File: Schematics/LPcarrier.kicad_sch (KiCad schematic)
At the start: 46 parts, among them J284 Conn_01x04, J48 Conn_01x03, J49 Conn_01x04, J75 Conn_01x04, U241 LM78L05, U247 AMS1117-3.3, U248 PCF8574, U33 ADG409, U34 MCP4728, U35 ADG1204, U36 ADG1204, U55 TMUX6219, U57 TMUX6219

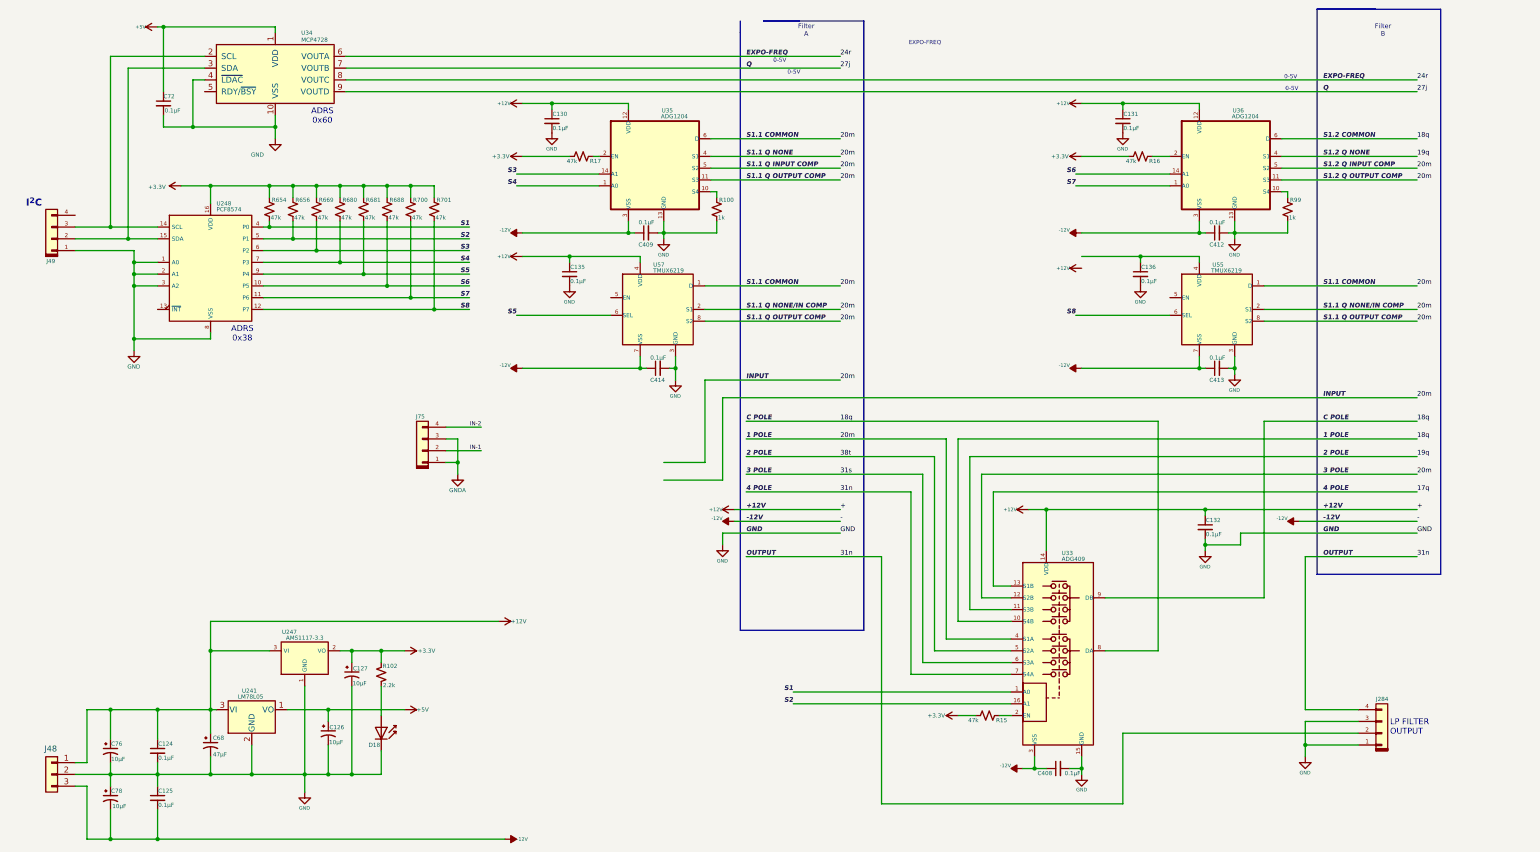
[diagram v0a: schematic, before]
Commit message: Corrected audio I/O on many schematics and added date to them.  Minor tweaks in voice interfaces.
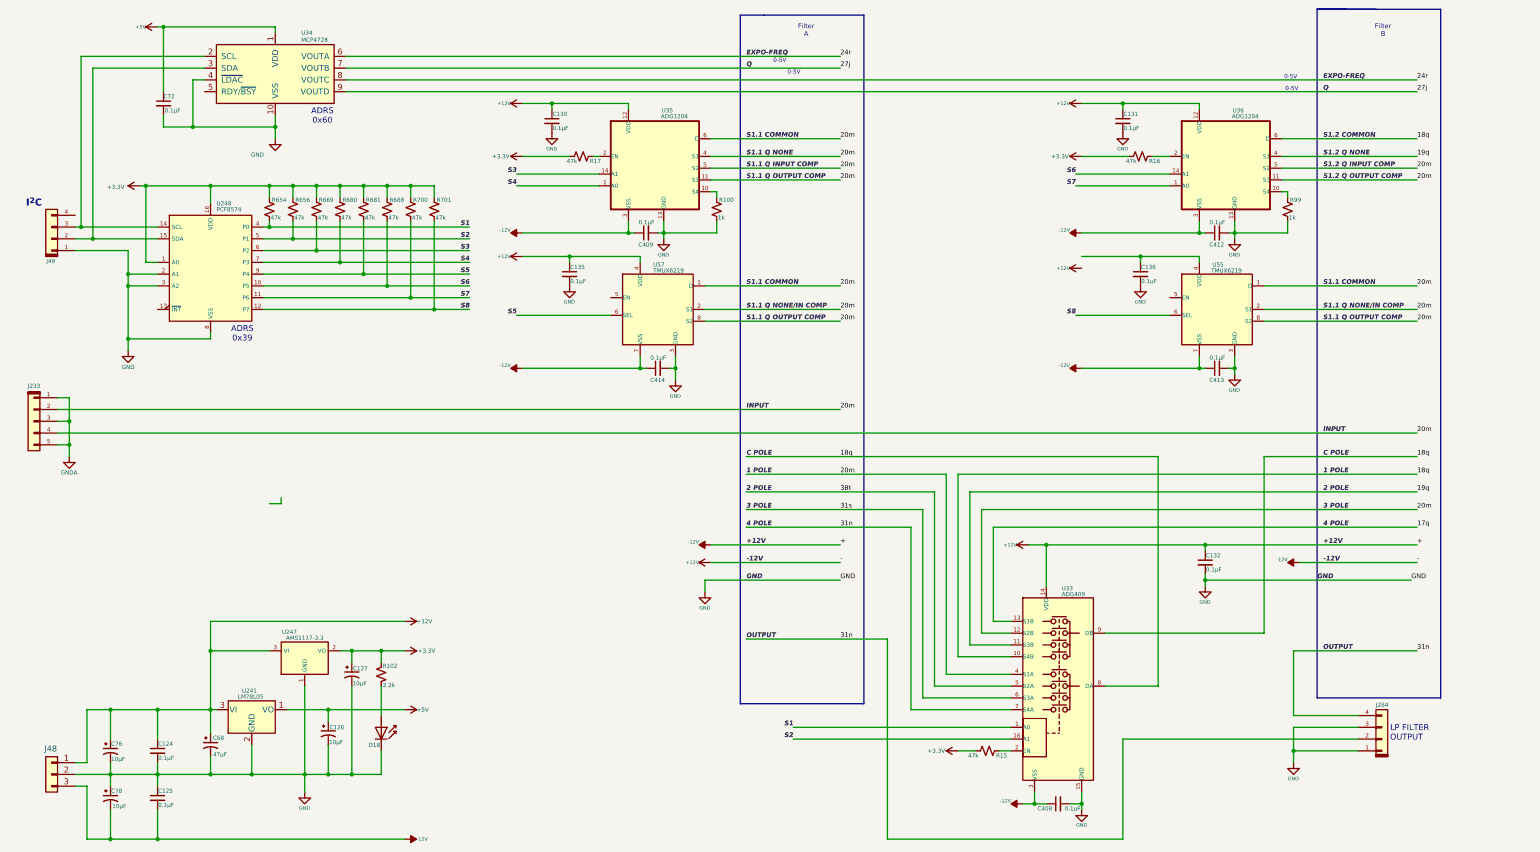
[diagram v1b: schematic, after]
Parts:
- removed J75: Conn_01x04, symbol My Connectors:Conn_01x04
- added J233: Conn_01x05, symbol My Connectors:Conn_01x05
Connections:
- net -12V is gone; now on net +12V: C125.2, C408.1, C409.1, C412.1, C413.1, C414.1, C78.2, J48.3 (Pin_3), U33.3 (VSS), U35.3 (VSS), U36.3 (VSS), U55.7 (VSS), U57.7 (VSS)
- net +3.3V: now also U248.1 (A0)
- net 1 POLE: now also J233.2 (Pin_2), J233.4 (Pin_4)
- net GND: no longer U248.1 (A0)
- net GNDA: now also J233.1 (Pin_1), J233.3 (Pin_3), J233.5 (Pin_5)
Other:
- note added: "ADRS 0x39"
- note removed: "ADRS 0x38"
- note removed: "EXPO-FREQ"
- moved on the sheet: C132, C408, J284, R15, U33

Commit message: Updated schematics, adding new low pass fillter and, added some statistical synth data to monitor.
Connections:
- net +12V: now also C136.1, U55.4 (VDD)
- net 1 POLE: now also U33.13 (S1B); no longer J233.2 (Pin_2), J233.4 (Pin_4), U33.10 (S4B), U33.12 (S2B), U33.6 (S3A), U33.8 (DA), U33.9 (DB), U35.11 (S3), U35.4 (S1), U35.5 (S2), U35.6 (D), U36.11 (S3), U36.5 (S2), U36.6 (D), U55.1 (D), U55.2 (S1), U55.8 (S2), U57.1 (D), U57.2 (S1), U57.8 (S2)
- net S3: now also U35.1 (A0); no longer U35.14 (A1)
- net S4: now also U35.14 (A1); no longer U35.1 (A0)
- net S5: now also U36.1 (A0); no longer U57.6 (SEL)
- net S7: now also U55.6 (SEL); no longer U36.1 (A0)
- net S8: now also U57.6 (SEL); no longer U55.6 (SEL)
- net 17q renamed 30d
- net 30d: no longer U33.13 (S1B), U33.7 (S4A)
- removed net 19q: U33.11 (S3B), U33.5 (S2A), U36.4 (S1)
- net 24r renamed 14k
- net 27j renamed 15j
- new net 17a: U36.6 (D)
- new net 18a: U36.5 (S2)
- new net 19a: U36.4 (S1)
- new net 19j: U36.11 (S3)
- new net 2 POLE: U33.12 (S2B), U33.5 (S2A)
- new net 24b: U35.11 (S3), U55.8 (S2), U57.8 (S2)
- new net 24g: U35.6 (D), U55.1 (D), U57.1 (D)
- new net 25h: U55.2 (S1), U57.2 (S1)
- new net 3 POLE: U33.11 (S3B), U33.6 (S3A)
- new net 4 POLE: U33.10 (S4B), U33.7 (S4A)
- new net 40b: U33.8 (DA), U33.9 (DB)
- new net 52q: J233.2 (Pin_2), J233.4 (Pin_4)
- new net 53a: U35.5 (S2)
- new net 54a: U35.4 (S1)
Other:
- note added: "Black"
- note added: "Blue"
- note added: "Brown"
- note added: "Green"
- note added: "LP FILTER INPUT"
- note added: "Orange"
- note added: "Red"
- note added: "Violet"
- note added: "Yellow"
- moved on the sheet: C124, C125, C126, C127, C68, C76, C78, D18, J233, J284, J48, J49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
